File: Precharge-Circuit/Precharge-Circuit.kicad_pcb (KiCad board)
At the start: 2 copper layers, 0 parts

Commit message: フットプリント追加
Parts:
- added C1: 0.1u_1608, Capacitor_SMD:C_0603_1608Metric, F.Cu at (151.2, 133.9)
- added C2: 10u_3216, Capacitor_SMD:C_1206_3216Metric, F.Cu at (188.4, 139.6)
- added C3: 0.1u_1608, Capacitor_SMD:C_0603_1608Metric, F.Cu at (151.2, 136.4)
- added C4: 0.1u_1608, Capacitor_SMD:C_0603_1608Metric, F.Cu at (151.2, 138.9)
- added C5: 1000p_3216, Capacitor_SMD:C_1206_3216Metric, F.Cu at (188.4, 143.0)
- added D1: PZ1AH11B-AU, ProjectEV:D_SOD-123HE_PZ1AHxxxB-AU, F.Cu at (188.9, 146.3)
- added D10: LED, LED_SMD:LED_0603_1608Metric, F.Cu at (173.0, 144.3)
- added D11: BZT52H-C16, ProjectEV:D_SOD-123F_BZT52H-xxx, F.Cu at (187.4, 65.2)
- added D12: BZT52H-C16, ProjectEV:D_SOD-123F_BZT52H-xxx, F.Cu at (187.4, 68.3)
- added D13: BZT52H-C16, ProjectEV:D_SOD-123F_BZT52H-xxx, F.Cu at (187.4, 71.5)
- added D14: BZT52H-C16, ProjectEV:D_SOD-123F_BZT52H-xxx, F.Cu at (187.4, 74.6)
- added D15: 1N4448WQ-7-F, ProjectEV:D_SOD-123_1N4448W, F.Cu at (168.1, 137.4)
- added D16: BZT52H-C16, ProjectEV:D_SOD-123F_BZT52H-xxx, F.Cu at (187.4, 77.8)
- added D17: 1N4448WQ-7-F, ProjectEV:D_SOD-123_1N4448W, F.Cu at (168.1, 140.5)
- added D18: BZT52H-C16, ProjectEV:D_SOD-123F_BZT52H-xxx, F.Cu at (187.4, 80.9)
- added D19: LED, LED_SMD:LED_0603_1608Metric, F.Cu at (173.0, 146.9)
- added D2: 1N4448WQ-7-F, ProjectEV:D_SOD-123_1N4448W, F.Cu at (168.1, 134.2)
- added D20: DFLZ24Q-7, ProjectEV:D_PowerDI-123_DFLZxxQ, F.Cu at (140.9, 146.6)
- added D21: 1N4448WQ-7-F, ProjectEV:D_SOD-123_1N4448W, F.Cu at (168.1, 143.7)
- added D22: 1N4448WQ-7-F, ProjectEV:D_SOD-123_1N4448W, F.Cu at (168.1, 146.8)
- added D3: LED, LED_SMD:LED_0603_1608Metric, F.Cu at (173.0, 133.9)
- added D4: BZT52H-C16, ProjectEV:D_SOD-123F_BZT52H-xxx, F.Cu at (187.4, 55.7)
- added D5: BZT52H-C16, ProjectEV:D_SOD-123F_BZT52H-xxx, F.Cu at (187.4, 58.9)
- added D6: BZT52H-C16, ProjectEV:D_SOD-123F_BZT52H-xxx, F.Cu at (187.4, 62.0)
- added D7: LED, LED_SMD:LED_0603_1608Metric, F.Cu at (173.0, 136.5)
- added D8: LED, LED_SMD:LED_0603_1608Metric, F.Cu at (173.0, 139.1)
- added D9: LED, LED_SMD:LED_0603_1608Metric, F.Cu at (173.0, 141.7)
- added H1: M3, MountingHole:MountingHole_3.2mm_M3_Pad_Via, F.Cu at (181.6, 119.7)
- added H2: M3, MountingHole:MountingHole_3.2mm_M3_Pad_Via, F.Cu at (181.6, 127.6)
- added H3: M3, MountingHole:MountingHole_3.2mm_M3_Pad_Via, F.Cu at (181.6, 135.6)
- added H4: M3, MountingHole:MountingHole_3.2mm_M3_Pad_Via, F.Cu at (181.6, 143.5)
- added J1: S2P-VH, ProjectEV:Connector_S2P-VH, F.Cu at (154.0, 124.2)
- added J2: SM04B-PASS-1-TB, ProjectEV:Connector_SM04B-PASS-1-TB, F.Cu at (108.9, 141.9)
- added J3: SM02B-PASS-1-TB, ProjectEV:Connector_SM02B-PASS-1-TB, F.Cu at (133.0, 141.9)
- added J4: S2P-VH, ProjectEV:Connector_S2P-VH, F.Cu at (163.4, 124.2)
- added J5: S2P-VH, ProjectEV:Connector_S2P-VH, F.Cu at (172.9, 124.2)
- added J6: SM03B-PASS-1-TB, ProjectEV:Connector_SM03B-PASS-1-TB, F.Cu at (122.0, 141.9)
- added J7: 19427-0040, ProjectEV:Connector_MX150L_19427-0040, F.Cu at (125.6, 62.8)
- added J8: 19427-0040, ProjectEV:Connector_MX150L_19427-0040, F.Cu at (125.6, 104.1)
- added K1: G5Q-1A4_DC12, ProjectEV:Relay_G5Q-1A4 DC12, F.Cu at (182.2, 92.0)
- added K2: AZDC6-2AE-12D, ProjectEV:Relay_AZDC6-2AE-12D, F.Cu at (166.9, 70.2)
- added K3: G5Q-1A4_DC12, ProjectEV:Relay_G5Q-1A4 DC12, F.Cu at (182.2, 103.5)
- added Q1: DMP3098LQ-7, ProjectEV:Package_SOT-23_DMP3098LQ-7, F.Cu at (187.8, 117.9)
- added Q10: 2N7002K-AU, ProjectEV:Package_SOT-23_2N7002K-AU, F.Cu at (192.2, 135.7)
- added Q2: 2N7002K-AU, ProjectEV:Package_SOT-23_2N7002K-AU, F.Cu at (187.8, 122.4)
- added Q3: PJA3439-AU_R1_000A1, ProjectEV:Package_SOT-23_PJA3439-AU_R1_000A1, F.Cu at (187.8, 126.8)
- added Q4: 2N7002K-AU, ProjectEV:Package_SOT-23_2N7002K-AU, F.Cu at (187.8, 131.3)
- added Q5: PJA3439-AU_R1_000A1, ProjectEV:Package_SOT-23_PJA3439-AU_R1_000A1, F.Cu at (187.8, 135.7)
- added Q6: 2N7002K-AU, ProjectEV:Package_SOT-23_2N7002K-AU, F.Cu at (192.2, 117.9)
- added Q7: PJA3439-AU_R1_000A1, ProjectEV:Package_SOT-23_PJA3439-AU_R1_000A1, F.Cu at (192.2, 122.4)
- added Q8: 2N7002K-AU, ProjectEV:Package_SOT-23_2N7002K-AU, F.Cu at (192.2, 126.8)
- added Q9: 2N7002K-AU, ProjectEV:Package_SOT-23_2N7002K-AU, F.Cu at (192.2, 131.3)
- added R1: 100k_1608, Resistor_SMD:R_0603_1608Metric, F.Cu at (151.2, 141.4)
- added R10: 1M_1608, Resistor_SMD:R_0603_1608Metric, F.Cu at (155.2, 146.4)
- added R11: 1M_1608, Resistor_SMD:R_0603_1608Metric, F.Cu at (155.2, 148.9)
- added R12: 10k_1608, Resistor_SMD:R_0603_1608Metric, F.Cu at (159.3, 133.9)
- added R13: 100_1608, Resistor_SMD:R_0603_1608Metric, F.Cu at (159.3, 136.4)
- added R14: 1M_1608, Resistor_SMD:R_0603_1608Metric, F.Cu at (159.3, 138.9)
- added R15: 100_1608, Resistor_SMD:R_0603_1608Metric, F.Cu at (159.3, 141.4)
- added R16: 100_1608, Resistor_SMD:R_0603_1608Metric, F.Cu at (159.3, 143.9)
- added R17: 100_1608, Resistor_SMD:R_0603_1608Metric, F.Cu at (159.3, 146.4)
- added R18: 10k_1608, Resistor_SMD:R_0603_1608Metric, F.Cu at (159.3, 148.9)
- added R19: 10k_1608, Resistor_SMD:R_0603_1608Metric, F.Cu at (163.3, 133.9)
- added R2: 100_1608, Resistor_SMD:R_0603_1608Metric, F.Cu at (151.2, 143.9)
- added R20: 1M_1608, Resistor_SMD:R_0603_1608Metric, F.Cu at (163.3, 136.4)
- added R21: 15k_5025, Resistor_SMD:R_2010_5025Metric, F.Cu at (152.9, 88.3)
- added R22: 15k_5025, Resistor_SMD:R_2010_5025Metric, F.Cu at (152.9, 92.5)
- added R23: 15k_5025, Resistor_SMD:R_2010_5025Metric, F.Cu at (152.9, 96.7)
- added R24: 15k_5025, Resistor_SMD:R_2010_5025Metric, F.Cu at (152.9, 100.9)
- added R25: 15k_5025, Resistor_SMD:R_2010_5025Metric, F.Cu at (152.9, 105.2)
- added R26: 1M_3216, Resistor_SMD:R_1206_3216Metric, F.Cu at (174.3, 111.0)
- added R27: 10k_1608, Resistor_SMD:R_0603_1608Metric, F.Cu at (163.3, 138.9)
- added R28: 15k_5025, Resistor_SMD:R_2010_5025Metric, F.Cu at (152.9, 109.4)
- added R29: 15k_5025, Resistor_SMD:R_2010_5025Metric, F.Cu at (152.9, 113.6)
- added R3: 1M_1608, Resistor_SMD:R_0603_1608Metric, F.Cu at (151.2, 146.4)
- added R30: 15k_5025, Resistor_SMD:R_2010_5025Metric, F.Cu at (160.3, 88.3)
- added R31: 15k_5025, Resistor_SMD:R_2010_5025Metric, F.Cu at (160.3, 92.5)
- added R32: 15k_5025, Resistor_SMD:R_2010_5025Metric, F.Cu at (160.3, 96.7)
- added R33: 1M_5025, Resistor_SMD:R_2010_5025Metric, F.Cu at (160.3, 100.9)
- added R34: 1M_5025, Resistor_SMD:R_2010_5025Metric, F.Cu at (160.3, 105.2)
- added R35: 1M_5025, Resistor_SMD:R_2010_5025Metric, F.Cu at (160.3, 109.4)
- added R36: 1M_5025, Resistor_SMD:R_2010_5025Metric, F.Cu at (160.3, 113.6)
- added R37: 82k_1608, Resistor_SMD:R_0603_1608Metric, F.Cu at (163.3, 141.4)
- added R38: 13k_1608, Resistor_SMD:R_0603_1608Metric, F.Cu at (163.3, 143.9)
- added R39: 1M_5025, Resistor_SMD:R_2010_5025Metric, F.Cu at (167.8, 88.3)
- added R4: 10k_1608, Resistor_SMD:R_0603_1608Metric, F.Cu at (151.2, 148.9)
- added R40: 1M_5025, Resistor_SMD:R_2010_5025Metric, F.Cu at (167.8, 92.5)
- added R41: 1M_5025, Resistor_SMD:R_2010_5025Metric, F.Cu at (167.8, 96.7)
- added R42: 1M_5025, Resistor_SMD:R_2010_5025Metric, F.Cu at (167.8, 100.9)
- added R5: 100_1608, Resistor_SMD:R_0603_1608Metric, F.Cu at (155.2, 133.9)
- added R6: 1M_1608, Resistor_SMD:R_0603_1608Metric, F.Cu at (155.2, 136.4)
- added R7: 10k_1608, Resistor_SMD:R_0603_1608Metric, F.Cu at (155.2, 138.9)
- added R8: 10k_1608, Resistor_SMD:R_0603_1608Metric, F.Cu at (155.2, 141.4)
- added R9: 10k_1608, Resistor_SMD:R_0603_1608Metric, F.Cu at (155.2, 143.9)
- added U1: TLP291(GB,SE, ProjectEV:Isolator_TLP291(GB,SE, F.Cu at (142.6, 138.7)
- added U2: TLP291(GB,SE, ProjectEV:Isolator_TLP291(GB,SE, F.Cu at (142.6, 142.9)
- added U3: TL431QDBVR, ProjectEV:Package_SOT-23-5_TL431QDBVR, F.Cu at (192.8, 56.4)
- added U4: TL431QDBVR, ProjectEV:Package_SOT-23-5_TL431QDBVR, F.Cu at (192.8, 60.8)

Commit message: 更新
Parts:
- added R17: 10k_1608, Resistor_SMD:R_0603_1608Metric, F.Cu at (140.7, 162.4)
- added R18: 10k_1608, Resistor_SMD:R_0603_1608Metric, F.Cu at (140.7, 165.0)
- added R19: 10k_1608, Resistor_SMD:R_0603_1608Metric, F.Cu at (140.7, 167.5)
- added R20: 10k_1608, Resistor_SMD:R_0603_1608Metric, F.Cu at (140.7, 170.0)
- added R21: 10k_1608, Resistor_SMD:R_0603_1608Metric, F.Cu at (140.7, 172.5)
- added R26: 10k_1608, Resistor_SMD:R_0603_1608Metric, F.Cu at (140.7, 175.0)
- added R3: 10k_1608, Resistor_SMD:R_0603_1608Metric, F.Cu at (156.0, 113.5)
- added R7: 10k_1608, Resistor_SMD:R_0603_1608Metric, F.Cu at (140.7, 157.4)
- added R8: 10k_1608, Resistor_SMD:R_0603_1608Metric, F.Cu at (140.7, 159.9)
- moved D11 107.2 mm to (80.9, 89.4)
- moved D13 107.2 mm to (80.9, 76.8)
- moved D14 107.2 mm to (80.9, 80.0)
- moved D15 107.2 mm to (80.9, 83.1)
- moved D16 107.2 mm to (80.9, 86.2)
- moved D17 107.2 mm to (80.9, 92.5)
- moved D5 107.2 mm to (80.9, 73.7)
- moved D6 107.2 mm to (80.9, 70.5)
- moved H1 100.2 mm to (105.0, 55.0)
- moved Q1 86.4 mm to (136.5, 187.5), turned to 90 degrees
- moved H4 76.6 mm to (105.0, 145.0)
- moved H2 73.8 mm to (195.0, 55.0)
- moved J1 68.9 mm to (96.0, 161.5), turned to -90 degrees
- moved J8 67.3 mm to (191.0, 88.5), turned to 90 degrees
- moved C1 67.1 mm to (143.5, 189.5), turned to -90 degrees
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- renumbered C2 to C1, C1 to C2, D16 to D11, D15 to D12, D11 to D13, D12 to D14, D13 to D15, D14 to D16, D18 to D17, D17 to D18, D4 to D2, D2 to D3, D3 to D4, D6 to D5, D5 to D6, R6 to R10, R8 to R11, R9 to R12, R12 to R13, R10 to R14, R11 to R15, R13 to R16, R15 to R22, R16 to R23, R14 to R24, R17 to R25, R18 to R27, R19 to R28, R20 to R29, R21 to R30, R22 to R31, R23 to R32, R24 to R33, R25 to R34, R26 to R35, R27 to R36, R28 to R37, R29 to R38, R30 to R39, R5 to R4, R31 to R40, R32 to R41, R33 to R42, R34 to R43, R35 to R44, R36 to R45, R37 to R46, R38 to R47, R39 to R48, R40 to R49, R4 to R5, R41 to R50, R42 to R51, R3 to R6, R7 to R9
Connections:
- net Net-(J3-Pin_1) renamed /V_{supply}
- D11 pad 2: GND -> Net-(D11-A)
- D13 pad 1: +12V -> Net-(D13-K)
- D14 pad 2: GND -> Net-(D14-A)
- D15 pad 1: +12V -> Net-(D15-K)
- D16 pad 2: GND -> Net-(D16-A)
- D17 pad 2: GND -> Net-(D17-A)
- D2 pad 2: GND -> Net-(D2-A)
- D5 pad 2: GND -> Net-(D5-A)
- D6 pad 1: /SDN_IN -> Net-(D6-K)

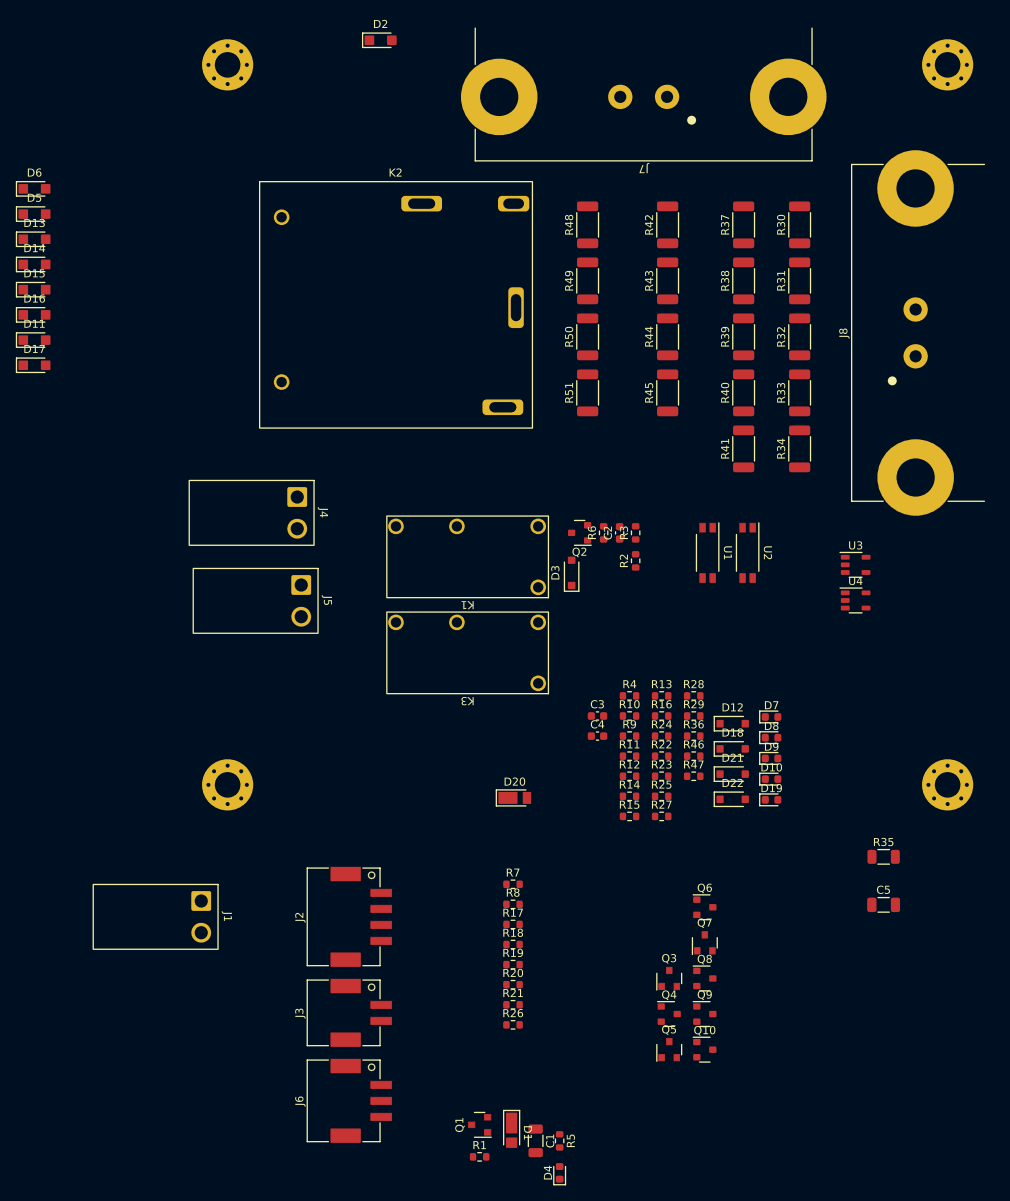
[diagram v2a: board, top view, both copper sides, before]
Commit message: パーツ配置、ピンアサイン変更
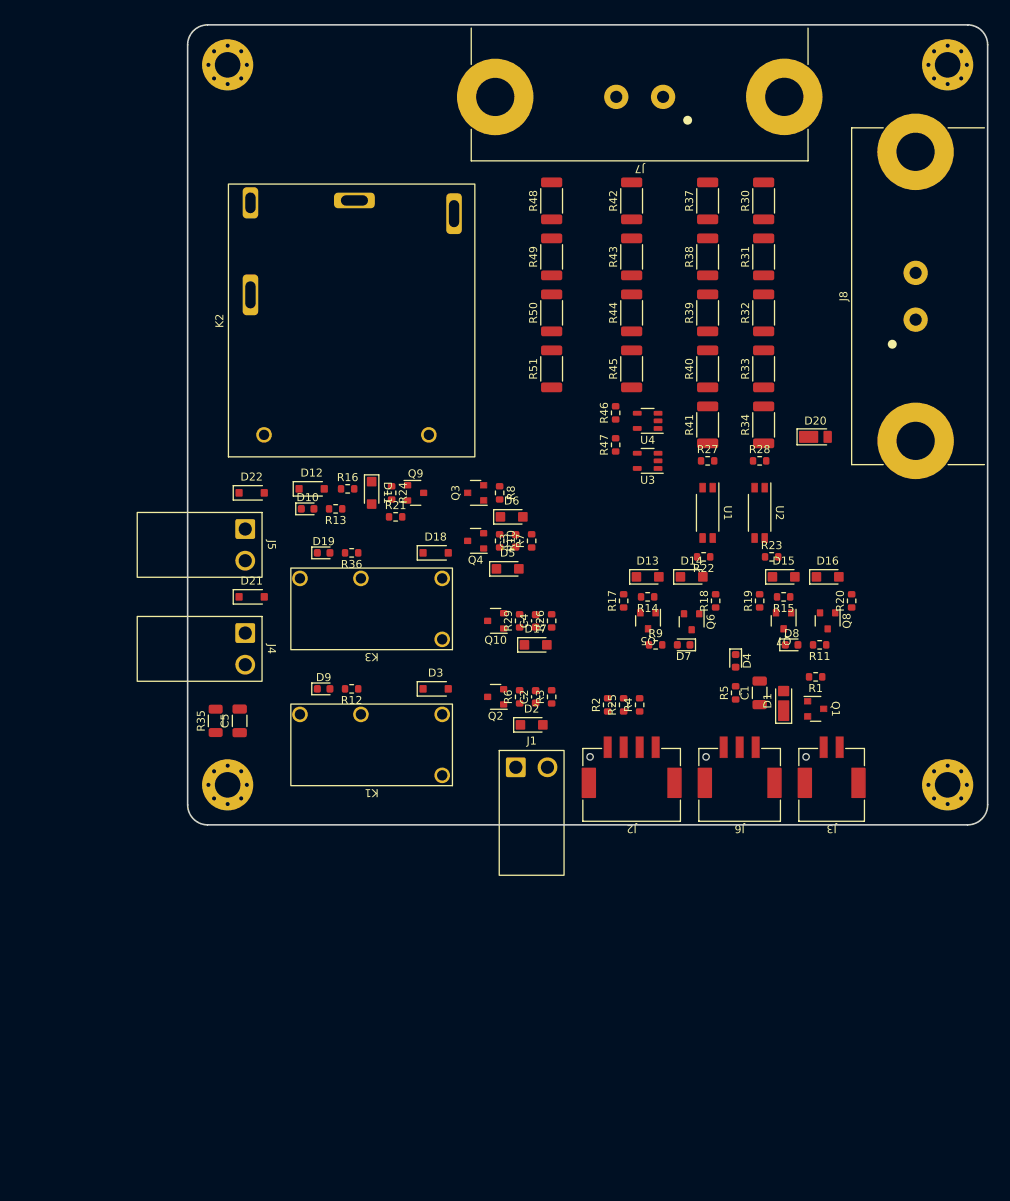
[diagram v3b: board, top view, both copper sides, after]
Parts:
- moved D16 104.4 mm to (180.0, 119.0)
- moved D15 100.3 mm to (174.5, 119.0)
- moved D14 91.0 mm to (163.0, 119.0)
- moved D2 87.6 mm to (143.0, 137.5)
- moved D13 87.5 mm to (157.5, 119.0)
- moved R35 85.2 mm to (103.5, 137.0), turned to 90 degrees
- moved C5 83.7 mm to (106.5, 137.0), turned to 90 degrees
- moved Q9 74.5 mm to (128.5, 108.5)
- moved D5 73.9 mm to (140.0, 118.0)
- moved R1 73.2 mm to (178.5, 131.5), turned to 180 degrees
- moved D6 72.4 mm to (140.5, 111.5)
- moved D17 71.7 mm to (143.5, 127.5)
- moved D22 71.3 mm to (108.0, 108.5)
- moved D4 67.7 mm to (168.5, 129.5), turned to -90 degrees
- moved J3 67.3 mm to (180.5, 145.0), turned to 180 degrees
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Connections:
- J2 pad 2: /~{PCHG_EN} -> /AIR-_EN
- J2 pad 3: /AIR-_EN -> /~{PCHG_EN}
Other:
- board outline added: 100 x 100 mm

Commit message: パーツ配置
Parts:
- moved D4 19.5 mm to (177.0, 147.0), turned to 90 degrees
- moved D9 17.8 mm to (103.0, 122.0)
- moved R12 17.8 mm to (106.5, 122.0)
- moved D19 15.7 mm to (103.0, 109.0)
- moved R36 15.7 mm to (106.5, 109.0)
- moved R14 15.6 mm to (168.0, 133.0), turned to 90 degrees
- moved R17 15.4 mm to (168.0, 129.5)
- moved R5 13.1 mm to (177.0, 143.5), turned to -90 degrees
- moved R11 13.1 mm to (169.5, 136.5), turned to 0 degrees
- moved D10 12.8 mm to (103.0, 106.0)
- moved R13 12.8 mm to (106.5, 106.0)
- moved R15 11.5 mm to (174.5, 133.0), turned to 90 degrees
- moved D13 11.4 mm to (166.5, 126.0), turned to 180 degrees
- moved Q5 11.3 mm to (165.0, 133.0), turned to 90 degrees
- moved D18 10.8 mm to (137.0, 125.0), turned to 90 degrees
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
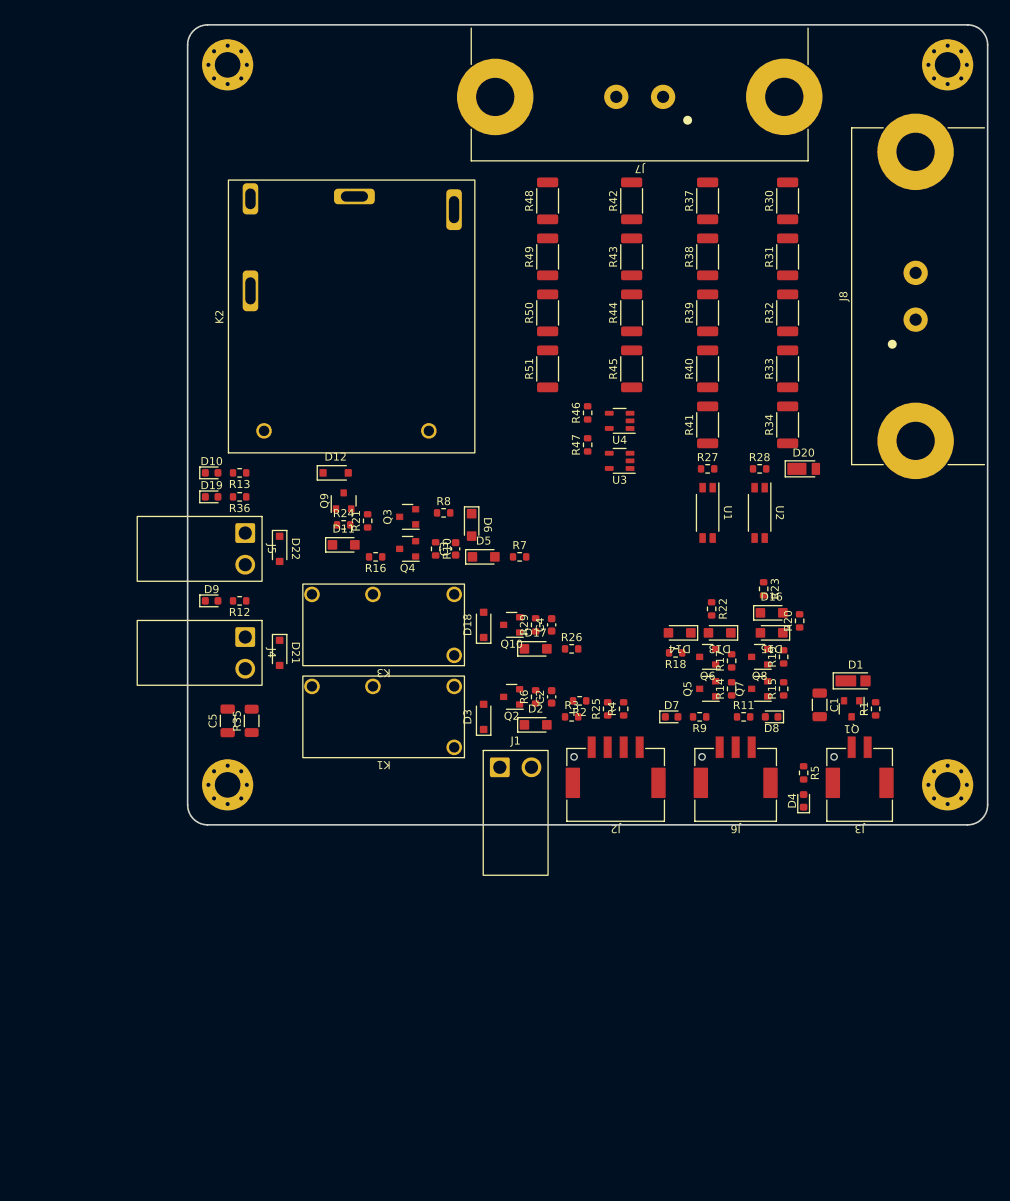
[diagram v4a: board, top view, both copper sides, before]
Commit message: NOT ゲートの電流制限抵抗追加、高電圧コネクタフットプリント更新、配線GNDベタ以外
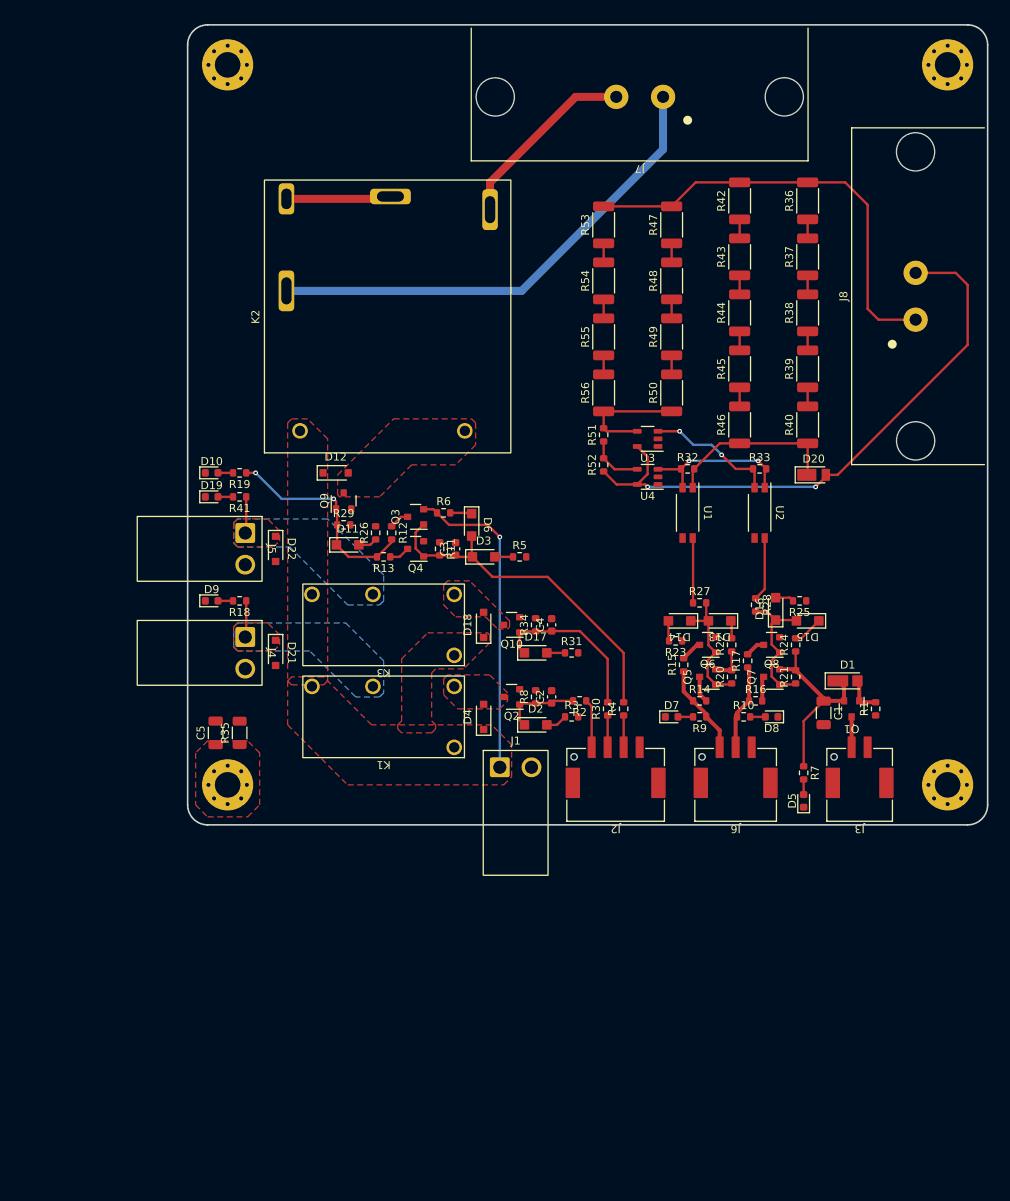
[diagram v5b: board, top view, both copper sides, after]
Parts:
- added R13: 100_1608, Resistor_SMD:R_0603_1608Metric, F.Cu at (124.5, 116.5)
- added R14: 100_1608, Resistor_SMD:R_0603_1608Metric, F.Cu at (164.0, 134.5)
- added R15: 100_1608, Resistor_SMD:R_0603_1608Metric, F.Cu at (162.0, 130.0)
- added R16: 100_1608, Resistor_SMD:R_0603_1608Metric, F.Cu at (171.0, 134.5)
- added R17: 100_1608, Resistor_SMD:R_0603_1608Metric, F.Cu at (170.0, 129.5)
- moved U4 7.83 mm to (157.5, 106.5)
- moved R53 7.62 mm to (152.0, 75.0)
- moved R54 7.62 mm to (152.0, 82.0)
- moved R55 7.62 mm to (152.0, 89.0)
- moved R56 7.62 mm to (152.0, 96.0)
- moved R47 5.83 mm to (160.5, 75.0)
- moved R48 5.83 mm to (160.5, 82.0)
- moved R49 5.83 mm to (160.5, 89.0)
- moved R50 5.83 mm to (160.5, 96.0)
- moved D15 4.74 mm to (177.5, 124.5)
- moved K2 4.50 mm to (125.0, 86.5)
- moved U3 4.45 mm to (157.5, 101.8)
- moved R42 4.00 mm to (169.0, 72.0)
- moved R43 4.00 mm to (169.0, 79.0)
- moved R44 4.00 mm to (169.0, 86.0)
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- renumbered D5 to D3, D3 to D4, D4 to D5, R11 to R10, R10 to R11, R16 to R12, R12 to R18, R13 to R19, R14 to R20, R15 to R21, R17 to R22, R18 to R23, R19 to R24, R20 to R25, R21 to R26, R22 to R27, R23 to R28, R24 to R29, R25 to R30, R26 to R31, R27 to R32, R28 to R33, R29 to R34, R30 to R36, R31 to R37, R32 to R38, R33 to R39, R34 to R40, R36 to R41, R37 to R42, R38 to R43, R39 to R44, R40 to R45, R41 to R46, R42 to R47, R43 to R48, R44 to R49, R7 to R5, R45 to R50, R46 to R51, R47 to R52, R48 to R53, R49 to R54, R50 to R55, R51 to R56, R8 to R6, R5 to R7, R6 to R8
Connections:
- Q4 pad 3: Net-(Q3-D) -> Net-(Q4-D)
- Q5 pad 3: /Voltage_Detect_1 -> Net-(Q5-D)
- Q6 pad 3: /Voltage_Detect_1 -> Net-(Q6-D)
- Q7 pad 3: /Voltage_Detect_2 -> Net-(Q7-D)
- Q8 pad 3: /Voltage_Detect_2 -> Net-(Q8-D)
- R19 pad 1: Net-(Q3-D) -> Net-(D11-K)
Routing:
- net /TS-: track 0.00 -> 74.2 mm, vias 0 -> 2
- net /PCHG_IN: track 0.00 -> 61.0 mm
- net /TS+: track 0.00 -> 55.0 mm
- net Net-(D3-K): track 0.00 -> 43.8 mm
- net /SDN_IN: track 0.00 -> 39.7 mm, vias 0 -> 1
- net +12V: track 0.00 -> 28.7 mm
- net Net-(D11-K): track 0.00 -> 26.9 mm, vias 0 -> 2
- net /PCHG_OUT: track 0.00 -> 23.6 mm
- net Net-(D20-K): track 0.00 -> 21.9 mm
- net Net-(D17-K): track 0.00 -> 20.7 mm
- net Net-(U1-Cathode): track 0.00 -> 19.2 mm, vias 0 -> 2
- net Net-(D15-A): track 0.00 -> 17.1 mm
- net Net-(U2-Cathode): track 0.00 -> 16.3 mm, vias 0 -> 2
- net Net-(D13-A): track 0.00 -> 15.8 mm
- net Net-(U3-REF): track 0.00 -> 15.0 mm
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- added copper zone on B.Cu, net /AIR+_Drive
- added copper zone on F.Cu, net /AIR+_Drive
- added copper zone on B.Cu, net /AIR-_DRIVE
- added copper zone on F.Cu, net /AIR-_DRIVE
- added copper zone on F.Cu, net /SDN_IN
- added copper zone on F.Cu, net Net-(C5-Pad1)
- added copper zone on F.Cu, net Net-(D12-A)
- added copper zone on F.Cu, net Net-(D18-A)
- added copper zone on F.Cu, net Net-(D4-A)
